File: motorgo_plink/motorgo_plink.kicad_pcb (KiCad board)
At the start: 4 copper layers, 65.2 x 56 mm, 0 parts

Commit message: WIP update. Layout begin
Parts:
- added C1: DNP, Capacitor_SMD:C_0402_1005Metric, F.Cu at (16.8, 80.9)
- added C10: 100uF, Capacitor_SMD:C_1210_3225Metric, F.Cu at (125.4, 105.6)
- added C11: 0.1uF, Capacitor_SMD:C_0402_1005Metric, B.Cu at (153.5, 107.1)
- added C12: 0.1uF, Capacitor_SMD:C_0402_1005Metric, B.Cu at (153.4, 108.1)
- added C13: .022uF, Capacitor_SMD:C_0402_1005Metric, B.Cu at (153.0, 105.6)
- added C14: 100uF, Capacitor_SMD:C_1210_3225Metric, F.Cu at (154.6, 105.6)
- added C15: 10uF 4mOhm, Capacitor_SMD:C_0805_2012Metric, F.Cu at (157.9, 85.0)
- added C16: 220uF 50v, Capacitor_SMD:CP_Elec_10x10, F.Cu at (52.7, 67.8)
- added C17: 4.7uF 1mOhm, Capacitor_SMD:C_0603_1608Metric, F.Cu at (152.4, 86.4)
- added C18: 2.2nF 0Ohm, Capacitor_SMD:C_0201_0603Metric, F.Cu at (161.3, 84.4)
- added C2: DNP, Capacitor_SMD:C_0402_1005Metric, F.Cu at (16.8, 82.9)
- added C20: 43pF 0Ohm, Capacitor_SMD:C_0201_0603Metric, F.Cu at (161.3, 86.2)
- added C21: 1uF, Capacitor_SMD:C_0603_1608Metric, F.Cu at (165.0, 98.3)
- added C22: 100nf 280mOhm, Capacitor_SMD:C_0402_1005Metric, F.Cu at (148.9, 84.3)
- added C23: 47uF 1mOhm, Capacitor_SMD:C_1210_3225Metric, F.Cu at (158.5, 81.4)
- added C24: 22uF 16v, Capacitor_SMD:C_0603_1608Metric, F.Cu at (135.8, 91.7)
- added C25: 22uF 16v, Capacitor_SMD:C_0603_1608Metric, F.Cu at (135.7, 94.7)
- added C26: 0.1uF, Capacitor_SMD:C_0402_1005Metric, B.Cu at (168.1, 107.1)
- added C27: 0.1uF, Capacitor_SMD:C_0402_1005Metric, B.Cu at (168.1, 108.1)
- added C28: .022uF, Capacitor_SMD:C_0402_1005Metric, B.Cu at (167.6, 105.6)
- added C29: 100uF, Capacitor_SMD:C_1210_3225Metric, F.Cu at (169.2, 105.6)
- added C3: 0.1uF, Capacitor_SMD:C_0402_1005Metric, B.Cu at (139.0, 107.1)
- added C30: 100nF, Capacitor_SMD:C_01005_0402Metric, F.Cu at (81.7, 38.1)
- added C31: 100nF, Capacitor_SMD:C_01005_0402Metric, F.Cu at (81.7, 39.7)
- added C32: 1uF, Capacitor_SMD:C_0603_1608Metric, F.Cu at (70.5, 48.4)
- added C4: 0.1uF, Capacitor_SMD:C_0402_1005Metric, B.Cu at (139.0, 108.1)
- added C5: .022uF, Capacitor_SMD:C_0402_1005Metric, B.Cu at (138.6, 105.6)
- added C6: 100uF, Capacitor_SMD:C_1210_3225Metric, F.Cu at (140.2, 105.6)
- added C7: 0.1uF, Capacitor_SMD:C_0402_1005Metric, B.Cu at (124.3, 107.1)
- added C8: 0.1uF, Capacitor_SMD:C_0402_1005Metric, B.Cu at (124.3, 108.1)
- added C9: .022uF, Capacitor_SMD:C_0402_1005Metric, B.Cu at (123.8, 105.6)
- added D1: LED, LED_SMD:LED_0805_2012Metric, F.Cu at (38.3, 77.7)
- added D2: LED, LED_SMD:LED_0805_2012Metric, F.Cu at (38.3, 80.8)
- added D3: LED, LED_SMD:LED_0805_2012Metric, F.Cu at (38.3, 83.8)
- added J1: USB4520-03-0-A_REVA, mg_mini_v1r3:GCT_USB4520-03-0-A_REVA, F.Cu at (172.5, 77.8)
- added J10: Conn_01x02_Pin, Connector_PinHeader_2.54mm:PinHeader_1x02_P2.54mm_Vertical, F.Cu at (143.8, 114.1)
- added J11: ~, LCSC_parts:CONN-TH_DC-005-2.5A-2.0, F.Cu at (120.7, 97.8)
- added J12: USB4520-03-0-A_REVA, mg_mini_v1r3:GCT_USB4520-03-0-A_REVA, F.Cu at (172.4, 94.5)
- added J13: I2C_STANDARDQWIIC, Connector_JST:JST_SH_BM04B-SRSS-TB_1x04-1MP_P1.00mm_Vertical, F.Cu at (29.1, 90.5)
- added J14: BM05B-SRSS-TB_LF__SN_, SnapEDA Library:JST_BM05B-SRSS-TB_LF__SN_, F.Cu at (119.4, 114.7)
- added J15: I2C_STANDARDQWIIC, Connector_JST:JST_SH_BM04B-SRSS-TB_1x04-1MP_P1.00mm_Vertical, F.Cu at (29.1, 96.7)
- added J16: BM05B-SRSS-TB_LF__SN_, SnapEDA Library:JST_BM05B-SRSS-TB_LF__SN_, F.Cu at (133.9, 114.7)
- added J17: I2C_STANDARDQWIIC, Connector_JST:JST_SH_BM04B-SRSS-TB_1x04-1MP_P1.00mm_Vertical, F.Cu at (29.1, 103.0)
- added J18: BM05B-SRSS-TB_LF__SN_, SnapEDA Library:JST_BM05B-SRSS-TB_LF__SN_, F.Cu at (149.8, 114.7)
- added J19: I2C_STANDARDQWIIC, Connector_JST:JST_SH_BM04B-SRSS-TB_1x04-1MP_P1.00mm_Vertical, F.Cu at (29.1, 109.2)
- added J2: ~, Button_Switch_SMD:SW_SPST_TL3342, F.Cu at (40.9, 55.7)
- added J20: BM05B-SRSS-TB_LF__SN_, SnapEDA Library:JST_BM05B-SRSS-TB_LF__SN_, F.Cu at (164.5, 114.7)
- added J22: Conn_01x02_Pin, Connector_PinHeader_2.54mm:PinHeader_1x02_P2.54mm_Vertical, F.Cu at (158.4, 114.1)
- added J23: Conn_01x06_Pin, Connector_PinHeader_1.00mm:PinHeader_1x06_P1.00mm_Vertical, F.Cu at (78.9, 38.8)
- added J3: ~, Button_Switch_SMD:SW_SPST_TL3342, F.Cu at (40.9, 62.8)
- added J4: Conn_02x20_Odd_Even, Connector_PinHeader_2.54mm:PinHeader_2x20_P2.54mm_Vertical_SMD, F.Cu at (142.2, 64.0)
- added J4: Conn_02x20_Odd_Even, Connector_PinHeader_2.54mm:PinHeader_2x20_P2.54mm_Vertical_SMD, B.Cu at (142.2, 64.0)
- added J6: Conn_01x02_Pin, Connector_PinHeader_2.54mm:PinHeader_1x02_P2.54mm_Vertical, F.Cu at (139.9, 114.1)
- added J8: Conn_01x02_Pin, Connector_PinHeader_2.54mm:PinHeader_1x02_P2.54mm_Vertical, F.Cu at (125.4, 114.1)
- added JP1: DNP, Jumper:SolderJumper-2_P1.3mm_Open_RoundedPad1.0x1.5mm, F.Cu at (47.8, 54.0)
- added JP2: DNP, Jumper:SolderJumper-2_P1.3mm_Open_RoundedPad1.0x1.5mm, F.Cu at (47.8, 57.5)
- added JP3: DNP, Jumper:SolderJumper-2_P1.3mm_Open_RoundedPad1.0x1.5mm, F.Cu at (47.8, 61.1)
- added JP4: SolderJumper_2_Bridged, Jumper:SolderJumper-2_P1.3mm_Bridged2Bar_RoundedPad1.0x1.5mm, F.Cu at (164.7, 90.3)
- added JP5: SolderJumper_2_Open, Jumper:SolderJumper-2_P1.3mm_Open_RoundedPad1.0x1.5mm, F.Cu at (162.1, 90.3)
- added JP6: SolderJumper_2_Open, Jumper:SolderJumper-2_P1.3mm_Open_RoundedPad1.0x1.5mm, F.Cu at (159.4, 90.3)
- added L1: 3.3uH 14mOhm, LCSC_parts:IND-SMD_L7.3-W6.6, F.Cu at (155.4, 75.3)
- added Q1: SI2323, LCSC_parts:SI2323_SOT-23-3_L2.9-W1.3-P0.95-LS2.4-BR, F.Cu at (162.4, 98.1)
- added R1: 1k, Resistor_SMD:R_0402_1005Metric, F.Cu at (42.0, 77.2)
- added R10: 10k, Resistor_SMD:R_0402_1005Metric, B.Cu at (128.8, 107.3)
- added R11: 10k, Resistor_SMD:R_0402_1005Metric, B.Cu at (128.9, 106.3)
- added R12: 10k, Resistor_SMD:R_0402_1005Metric, B.Cu at (114.1, 107.3)
- added R13: 10k, Resistor_SMD:R_0402_1005Metric, B.Cu at (114.1, 106.3)
- added R14: 10k, Resistor_SMD:R_0402_1005Metric, B.Cu at (143.3, 107.3)
- added R15: 10k, Resistor_SMD:R_0402_1005Metric, B.Cu at (143.3, 106.3)
- added R16: 102k, Resistor_SMD:R_0402_1005Metric, F.Cu at (148.9, 72.4)
- added R17: 36.5k, Resistor_SMD:R_0402_1005Metric, F.Cu at (148.9, 74.4)
- added R18: 53.6k, Resistor_SMD:R_0402_1005Metric, F.Cu at (148.9, 76.4)
- added R19: 3.4k, Resistor_SMD:R_0402_1005Metric, F.Cu at (148.9, 78.3)
- added R2: 1k, Resistor_SMD:R_0402_1005Metric, F.Cu at (42.0, 79.2)
- added R20: 10R 1%, Resistor_SMD:R_0402_1005Metric, F.Cu at (164.1, 96.1)
- added R21: DNP, Resistor_SMD:R_0402_1005Metric, F.Cu at (150.3, 97.7)
- added R22: DNP, Resistor_SMD:R_0402_1005Metric, F.Cu at (152.3, 97.7)
- added R23: 5.1K, Resistor_SMD:R_0402_1005Metric, F.Cu at (160.5, 99.2)
- added R24: 52.3k, Resistor_SMD:R_0402_1005Metric, F.Cu at (148.9, 80.3)
- added R25: 10k, Resistor_SMD:R_0402_1005Metric, F.Cu at (148.9, 82.3)
- added R26: 49.9K, Resistor_SMD:R_0402_1005Metric, F.Cu at (160.0, 97.7)
- added R27: 10K, Resistor_SMD:R_0402_1005Metric, F.Cu at (164.8, 87.8)
- added R28: 14K, Resistor_SMD:R_0402_1005Metric, F.Cu at (162.1, 87.8)
- added R29: 10.5K, Resistor_SMD:R_0402_1005Metric, F.Cu at (159.3, 87.8)
- added R3: 1k, Resistor_SMD:R_0402_1005Metric, F.Cu at (42.0, 81.2)
- added R30: 5k1, Resistor_SMD:R_0402_1005Metric, F.Cu at (35.0, 88.3)
- added R31: 5k1, Resistor_SMD:R_0402_1005Metric, F.Cu at (35.0, 90.3)
- added R32: 5k1, Resistor_SMD:R_0402_1005Metric, F.Cu at (35.0, 92.3)
- added R33: 5k1, Resistor_SMD:R_0402_1005Metric, F.Cu at (35.0, 94.3)
- added R34: 5k1, Resistor_SMD:R_0402_1005Metric, F.Cu at (35.0, 96.3)
- added R35: 5k1, Resistor_SMD:R_0402_1005Metric, F.Cu at (35.0, 98.3)
- added R36: 10k, Resistor_SMD:R_0402_1005Metric, B.Cu at (157.9, 107.3)
- added R37: 10k, Resistor_SMD:R_0402_1005Metric, B.Cu at (157.9, 106.3)
- added R38: 2k, Resistor_SMD:R_0402_1005Metric, F.Cu at (69.9, 38.2)
- added R39: 2k, Resistor_SMD:R_0402_1005Metric, F.Cu at (69.9, 40.2)
- added R4: 5k1, Resistor_SMD:R_0402_1005Metric, F.Cu at (44.9, 77.2)
- added R40: DNP, Resistor_SMD:R_0402_1005Metric, F.Cu at (69.9, 42.2)
- added R41: DNP, Resistor_SMD:R_0402_1005Metric, F.Cu at (69.9, 44.2)
- added R42: DNP, Resistor_SMD:R_0402_1005Metric, F.Cu at (69.9, 46.2)
- added R43: DNP, Resistor_SMD:R_0402_1005Metric, F.Cu at (72.8, 38.2)
- added R44: DNP, Resistor_SMD:R_0402_1005Metric, F.Cu at (72.8, 40.2)
- added R45: DNP, Resistor_SMD:R_0402_1005Metric, F.Cu at (72.8, 42.2)
- added R46: 1k, Resistor_SMD:R_0402_1005Metric, F.Cu at (72.8, 44.2)
- added R47: DNP, Resistor_SMD:R_0402_1005Metric, F.Cu at (72.8, 46.2)
- added R48: DNP, Resistor_SMD:R_0402_1005Metric, F.Cu at (75.7, 38.2)
- added R49: 1k, Resistor_SMD:R_0402_1005Metric, F.Cu at (75.7, 40.2)
- added R5: 5k1, Resistor_SMD:R_0402_1005Metric, F.Cu at (44.9, 79.2)
- added R50: 1k, Resistor_SMD:R_0402_1005Metric, F.Cu at (75.7, 42.2)
- added R6: 0, Resistor_SMD:R_0402_1005Metric, F.Cu at (44.9, 81.2)
- added R7: 0, Resistor_SMD:R_0402_1005Metric, F.Cu at (47.8, 77.2)
- added R8: 5k1, Resistor_SMD:R_0402_1005Metric, F.Cu at (47.8, 79.2)
- added R9: 5k1, Resistor_SMD:R_0402_1005Metric, F.Cu at (47.8, 81.2)
- added Rmode1: 20k, Resistor_SMD:R_0402_1005Metric, B.Cu at (128.8, 109.3)
- added Rmode2: 20k, Resistor_SMD:R_0402_1005Metric, B.Cu at (114.1, 109.3)
- added Rmode3: 20k, Resistor_SMD:R_0402_1005Metric, B.Cu at (143.3, 109.3)
- added Rmode4: 20k, Resistor_SMD:R_0402_1005Metric, B.Cu at (157.9, 109.3)
- added Rp1: 4.83k, Resistor_SMD:R_0402_1005Metric, B.Cu at (128.8, 108.3)
- added Rp2: 4.83k, Resistor_SMD:R_0402_1005Metric, B.Cu at (114.1, 108.3)
- added Rp3: 4.83k, Resistor_SMD:R_0402_1005Metric, B.Cu at (143.3, 108.3)
- added Rp4: 4.83k, Resistor_SMD:R_0402_1005Metric, B.Cu at (157.9, 108.3)
- added TP1: TestPoint, TestPoint:TestPoint_Pad_1.0x1.0mm, F.Cu at (133.2, 102.1)
- added TP10: TestPoint, TestPoint:TestPoint_Pad_1.0x1.0mm, F.Cu at (122.6, 102.1)
- added TP11: TestPoint, TestPoint:TestPoint_Pad_1.0x1.0mm, F.Cu at (151.8, 102.1)
- added TP12: TestPoint, TestPoint:TestPoint_Pad_1.0x1.0mm, F.Cu at (166.4, 102.1)
- added TP2: TestPoint, TestPoint:TestPoint_Pad_1.0x1.0mm, F.Cu at (118.5, 102.1)
- added TP3: TestPoint, TestPoint:TestPoint_Pad_1.0x1.0mm, F.Cu at (147.6, 102.1)
- added TP4: TestPoint, TestPoint:TestPoint_Pad_1.0x1.0mm, F.Cu at (162.3, 102.1)
- added TP5: TestPoint, TestPoint:TestPoint_Pad_1.0x1.0mm, F.Cu at (135.3, 102.1)
- added TP6: TestPoint, TestPoint:TestPoint_Pad_1.0x1.0mm, F.Cu at (120.5, 102.1)
- added TP7: TestPoint, TestPoint:TestPoint_Pad_1.0x1.0mm, F.Cu at (149.7, 102.1)
- added TP8: TestPoint, TestPoint:TestPoint_Pad_1.0x1.0mm, F.Cu at (164.3, 102.1)
- added TP9: TestPoint, TestPoint:TestPoint_Pad_1.0x1.0mm, F.Cu at (137.4, 102.1)
- added U1: ESP32-S3-WROOM-1, mg_mini_v1r3:ESP32-S3-WROOM-1, F.Cu at (122.8, 80.3)
- added U10: LIS3MDLTR, LCSC_parts:LIS3MDLTR_LGA-12, F.Cu at (74.3, 48.9)
- added U11: LSM6DS3TR, LCSC_parts:LSM6DSOTR_LGA-14, F.Cu at (79.2, 47.6)
- added U2: USBLC6-2P6, Package_TO_SOT_SMD:SOT-666, F.Cu at (163.7, 73.1)
- added U3: DRV8874PWPR, LCSC_parts:HTSSOP-16_L5.0-W4.4-P0.65-LS6.4-BL-EP, F.Cu at (134.3, 106.3)
- added U4: DRV8874PWPR, LCSC_parts:HTSSOP-16_L5.0-W4.4-P0.65-LS6.4-BL-EP, F.Cu at (119.6, 106.3)
- added U5: DRV8874PWPR, LCSC_parts:HTSSOP-16_L5.0-W4.4-P0.65-LS6.4-BL-EP, F.Cu at (148.7, 106.3)
- added U6: TPS54620RHLR, LCSC_parts:VQFN-14_L3.5-W3.5-P0.50-TL-EP_TPS54622RHLT, F.Cu at (153.0, 82.4)
- added U7: HUSB238_002DD, LCSC_parts:DFN-10_L3.0-W3.0-P0.50-BL-EP2.5, F.Cu at (163.5, 94.0)
- added U8: AMS1117-3.3, Package_TO_SOT_SMD:SOT-223-3_TabPin2, F.Cu at (130.5, 94.1)
- added U9: DRV8874PWPR, LCSC_parts:HTSSOP-16_L5.0-W4.4-P0.65-LS6.4-BL-EP, F.Cu at (163.4, 106.3)
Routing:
- net +3.3V: track 0.00 -> 62.9 mm, vias 0 -> 3
- net GND: track 0.00 -> 19.6 mm, vias 0 -> 8
- net /motor_controls4/motor_out1: track 0.00 -> 13.7 mm
- net +BATT: track 0.00 -> 12.4 mm, vias 0 -> 6
- net Net-(U9-PMODE): track 0.00 -> 10.0 mm, vias 0 -> 1
- net Net-(U9-nFAULT): track 0.00 -> 8.92 mm, vias 0 -> 3
- net +3V3: track 0.00 -> 8.57 mm, vias 0 -> 2
- net +VDC: track 0.00 -> 6.76 mm, vias 0 -> 3
- net Net-(U9-nSLEEP): track 0.00 -> 6.26 mm, vias 0 -> 2
- net Net-(U7-GATE): track 0.00 -> 6.18 mm
- net Net-(U9-IPROPI): track 0.00 -> 4.62 mm, vias 0 -> 1
- net Net-(U9-VCP): track 0.00 -> 3.95 mm, vias 0 -> 1
- net Net-(Q1-G): track 0.00 -> 3.87 mm
- net /motor_controls4/motor_out2: track 0.00 -> 3.79 mm
- net /Power Reg and Dist/CC1: track 0.00 -> 3.50 mm
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- added copper zone on In2.Cu, net +BATT
- added copper zone on In2.Cu, net +VDC
- added copper zone on In1.Cu, net GND
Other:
- board size 65.2 x 56 mm -> 80.2 x 56 mm

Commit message: WIP update. Ready for BOM editing
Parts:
- removed the J4 at (142.2, 64.0)
- removed R35: 5k1, Resistor_SMD:R_0402_1005Metric
- added J5: Conn_02x20_Odd_Even, Connector_PinSocket_2.54mm:PinSocket_2x20_P2.54mm_Vertical_SMD, B.Cu at (142.2, 64.0)
- J4: footprint Connector_PinHeader_2.54mm:PinHeader_2x20_P2.54mm_Vertical_SMD -> Connector_PinSocket_2.54mm:PinSocket_2x20_P2.54mm_Vertical_SMD
- R10, R11, R12, R13, R14, R15, R36, R37, Rmode1, Rmode2, Rmode3, Rmode4, Rp1, Rp2, Rp3, Rp4: moved to F.Cu
- R34: value 5k1 -> 0R0; footprint Resistor_SMD:R_0402_1005Metric -> Resistor_SMD:R_0603_1608Metric
- moved C2 142.9 mm to (159.6, 76.8)
- moved C1 142.8 mm to (159.6, 78.4)
- moved J3 122.5 mm to (161.6, 83.2)
- moved J2 121.9 mm to (161.6, 72.5)
- moved R4 119.1 mm to (164.0, 79.3)
- moved R5 119.0 mm to (163.9, 76.0)
- moved R6 117.0 mm to (161.9, 78.3)
- moved R34 114.9 mm to (148.2, 76.2)
- moved R7 114.0 mm to (161.9, 77.1)
- moved R8 109.0 mm to (156.7, 74.7), turned to 90 degrees
- moved R9 109.0 mm to (156.8, 81.1), turned to 90 degrees
- moved R32 101.1 mm to (134.5, 110.4)
- moved R33 98.7 mm to (132.4, 110.3), turned to 180 degrees
- moved D1 95.5 mm to (133.6, 84.0), turned to 180 degrees
- moved D3 95.3 mm to (133.6, 86.6), turned to 180 degrees
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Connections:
- C30 pad 1: GND -> GNDD
- C31 pad 1: +3V3 -> +3.3V
- C31 pad 2: GND -> GNDD
- C32 pad 1: +3V3 -> +3.3V
- C32 pad 2: GND -> GNDD
- R21 pad 1: +3V3 -> +3.3V
- R22 pad 1: +3V3 -> +3.3V
- R34 pad 1: +3.3V -> GNDD
- R34 pad 2: sda -> GND
- R38 pad 1: +3V3 -> +3.3V
- R39 pad 1: +3V3 -> +3.3V
- R40 pad 2: GND -> GNDD
- R41 pad 2: GND -> GNDD
- R42 pad 2: GND -> GNDD
- R43 pad 2: GND -> GNDD
- R44 pad 2: GND -> GNDD
- R45 pad 2: GND -> GNDD
- R46 pad 2: GND -> GNDD
- R47 pad 2: +3V3 -> +3.3V
- R48 pad 2: +3V3 -> +3.3V
- R49 pad 2: GND -> GNDD
- R50 pad 2: +3V3 -> +3.3V
- TP10 pad 1: +3V3 -> +3.3V
- TP11 pad 1: +3V3 -> +3.3V
- TP12 pad 1: +3V3 -> +3.3V
- TP9 pad 1: +3V3 -> +3.3V
- U10 pad 10: +3V3 -> +3.3V
- U10 pad 12: GND -> GNDD
- U10 pad 2: GND -> GNDD
- U10 pad 3: GND -> GNDD
- U10 pad 5: +3V3 -> +3.3V
- U10 pad 6: +3V3 -> +3.3V
- U11 pad 5: +3V3 -> +3.3V
- U11 pad 6: GND -> GNDD
- U11 pad 7: GND -> GNDD
- U11 pad 8: +3V3 -> +3.3V
- U3 pad 5: +3V3 -> +3.3V
- U4 pad 5: +3V3 -> +3.3V
- U5 pad 5: +3V3 -> +3.3V
- U6 pad 15: unconnected-(U6-EP-Pad15) -> GND
- U9 pad 5: +3V3 -> +3.3V
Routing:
- net +5V: track 3.47 -> 92.5 mm, vias 0 -> 16
- net enc_sda: track 0.00 -> 73.6 mm, vias 0 -> 5
- net GND: track 19.6 -> 93.0 mm, vias 8 -> 52
- net enc_scl: track 0.00 -> 70.4 mm, vias 0 -> 5
- net usb_d-: track 0.00 -> 55.5 mm, vias 0 -> 2
- net +BATT: track 12.4 -> 67.4 mm, vias 6 -> 21
- net +3.3V: track 62.9 -> 117.9 mm, vias 3 -> 18
- net usb_d+: track 0.00 -> 54.8 mm, vias 0 -> 2
- net m4_enc_cs: track 0.00 -> 52.1 mm, vias 0 -> 2
- net m4_PH: track 0.00 -> 41.5 mm, vias 0 -> 1
- net hidden_sda: track 0.00 -> 40.4 mm, vias 0 -> 7
- net m4_EN: track 0.00 -> 40.0 mm, vias 0 -> 1
- net hidden_scl: track 0.00 -> 38.9 mm, vias 0 -> 4
- net m3_enc_cs: track 0.00 -> 36.0 mm, vias 0 -> 1
- net m2_enc_cs: track 0.00 -> 29.8 mm, vias 0 -> 2
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- added copper zone on In2.Cu, net +3.3V
- added copper zone on In2.Cu, net +5V
- added copper zone on In1.Cu, net GNDD

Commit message: WIP update. change USBC port
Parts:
- removed J12: USB4520-03-0-A_REVA, mg_mini_v1r3:GCT_USB4520-03-0-A_REVA
- added D4: 20V 5A, LCSC_parts:D_SMB_LCSC_C5366311, B.Cu at (162.9, 96.3)
- added J7: USB4520-03-0-A_REVA, mg_mini_v1r3:USB-C-SMD_TYPEC-303-ACP16, F.Cu at (170.5, 94.2)
- J1: footprint mg_mini_v1r3:GCT_USB4520-03-0-A_REVA -> mg_mini_v1r3:USB-C-SMD_TYPEC-303-ACP16
- Rp1, Rp2, Rp3, Rp4: value 4.83k -> 4.87k
- moved R32 7.29 mm to (128.1, 113.9), turned to 90 degrees
- moved R33 4.86 mm to (129.1, 113.9), turned to 90 degrees
- moved R31 4.16 mm to (102.1, 108.0), turned to 180 degrees
- moved R30 2.40 mm to (102.1, 106.7), turned to 180 degrees
- moved J1 1.98 mm to (170.6, 77.5)
- moved R20 1.02 mm to (165.2, 96.1)
- moved R26 0.64 mm to (160.6, 97.7)
- moved Q1 0.45 mm to (162.7, 97.9), turned to 90 degrees
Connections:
- J4 pad 10: gpio43 -> gpio44
- J4 pad 8: gpio44 -> gpio43
- J5 pad 7: gpio44 -> gpio43
- J5 pad 9: gpio43 -> gpio44
- Q1 pad 2: +VDC -> Net-(D4-K)
- R26 pad 1: +VDC -> Net-(D4-K)
- U1 pad 10: m3_PH -> m2_PH
- U1 pad 11: m4_EN -> m2_EN
- U1 pad 12: gpio8 -> m3_PH
- U1 pad 15: gpio3 -> m3_EN
- U1 pad 17: gpio9 -> m3_enc_cs
- U1 pad 18: m1_EN -> m4_PH
- U1 pad 19: m1_PH -> m4_EN
- U1 pad 20: m2_EN -> m4_enc_cs
- U1 pad 21: m2_PH -> hidden_sda
- U1 pad 22: m3_EN -> hidden_scl
- U1 pad 23: m4_PH -> gpio38
- U1 pad 24: gpio47 -> gpio41
- U1 pad 25: m2_enc_cs -> gpio42
- U1 pad 28: enc_sda -> gpio4
- U1 pad 29: enc_scl -> gpio7
- U1 pad 30: m1_enc_cs -> gpio3
- U1 pad 31: gpio38 -> gpio8
- U1 pad 34: gpio41 -> gpio44
- U1 pad 35: gpio42 -> gpio47
- U1 pad 36: gpio44 -> gpio43
- U1 pad 37: gpio43 -> gpio9
- U1 pad 4: gpio4 -> m2_enc_cs
- U1 pad 5: hidden_scl -> m1_enc_cs
- U1 pad 6: hidden_sda -> enc_sda
- U1 pad 7: gpio7 -> enc_scl
- U1 pad 8: m3_enc_cs -> m1_PH
- U1 pad 9: m4_enc_cs -> m1_EN
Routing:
- net +3.3V: track 117.9 -> 211.8 mm, vias 18 -> 24
- net sda: track 0.00 -> 88.5 mm, vias 0 -> 5
- net scl: track 0.00 -> 85.5 mm, vias 0 -> 7
- net GND: track 93.0 -> 165.8 mm, vias 52 -> 75
- net boot: track 8.13 -> 64.4 mm, vias 0 -> 2
- net reset: track 8.29 -> 64.3 mm, vias 0 -> 2
- net gpio47: track 1.74 -> 55.3 mm, vias 0 -> 4
- net gpio38: track 5.40 -> 53.1 mm, vias 1 -> 4
- net gpio40: track 0.00 -> 47.1 mm, vias 0 -> 4
- net gpio39: track 0.00 -> 43.3 mm, vias 0 -> 2
- net gpio8: track 0.00 -> 35.3 mm, vias 0 -> 2
- net gpio41: track 0.00 -> 33.9 mm, vias 0 -> 2
- net gpio3: track 0.00 -> 31.4 mm, vias 0 -> 3
- net gpio42: track 0.00 -> 31.2 mm, vias 0 -> 2
- net hidden_sda: track 40.4 -> 69.6 mm, vias 7 -> 8
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- added copper zone on B.Cu, net +3.3V
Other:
- board size 80.2 x 56 mm -> 80.5 x 64.5 mm

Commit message: ready for order
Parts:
- removed C1, C2: DNP, Capacitor_SMD:C_0402_1005Metric
- moved C22 0.67 mm to (150.2, 90.8), turned to -90 degrees
- moved R17 0.37 mm to (153.0, 90.1)
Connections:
- J1 pad A12: (no net) -> GND
- J1 pad B1: (no net) -> GND
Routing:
- net +5V: track 118.0 -> 172.0 mm, vias 22 -> 26
- net +3.3V: track 211.8 -> 253.2 mm, vias 24 -> 29
- net GND: track 165.8 -> 191.3 mm, vias 75 -> 84
- net +BATT: track 66.6 -> 80.2 mm
- net Net-(C22-Pad1): track 0.50 -> 7.18 mm
- net gpio47: track 55.3 -> 56.8 mm
- net gpio38: track 53.1 -> 54.3 mm
- net gpio41: track 33.9 -> 34.6 mm
- net usb_d-: track 55.5 -> 55.0 mm
- net usb_d+: track 54.8 -> 54.2 mm
- net gpio40: track 47.1 -> 47.6 mm, vias 4 -> 3
- net gpio4: track 18.0 -> 17.7 mm, vias 2 -> 1
- net m4_EN: track 56.4 -> 56.6 mm, vias 2 -> 3
- net gpio42: vias 2 -> 1
- net gpio39: track 43.3 -> 43.4 mm, vias 2 -> 4
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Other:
- board text added: "Acc"
- board text added: "M3"
- board text added: "Mag"
- board text added: "X+"
- board text added: "Y+"
- board text added: "int1_a SDO_a int_mag"
- board text added: "int2_a drdy_mag SD0_mag"

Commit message: fix DRC errors
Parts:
- moved Rmode3 3.39 mm to (146.6, 109.9), turned to -135 degrees
- moved Rmode4 2.51 mm to (155.5, 110.2)
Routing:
- net +5V: track 172.0 -> 174.6 mm, vias 26 -> 23
- net Net-(U9-IMODE): track 2.86 -> 5.45 mm
- net GND: track 191.3 -> 190.5 mm, vias 84 -> 83
- net +3.3V: track 253.2 -> 252.7 mm
- net Net-(U5-IMODE): track 2.86 -> 2.35 mm
- net m4_EN: vias 3 -> 2

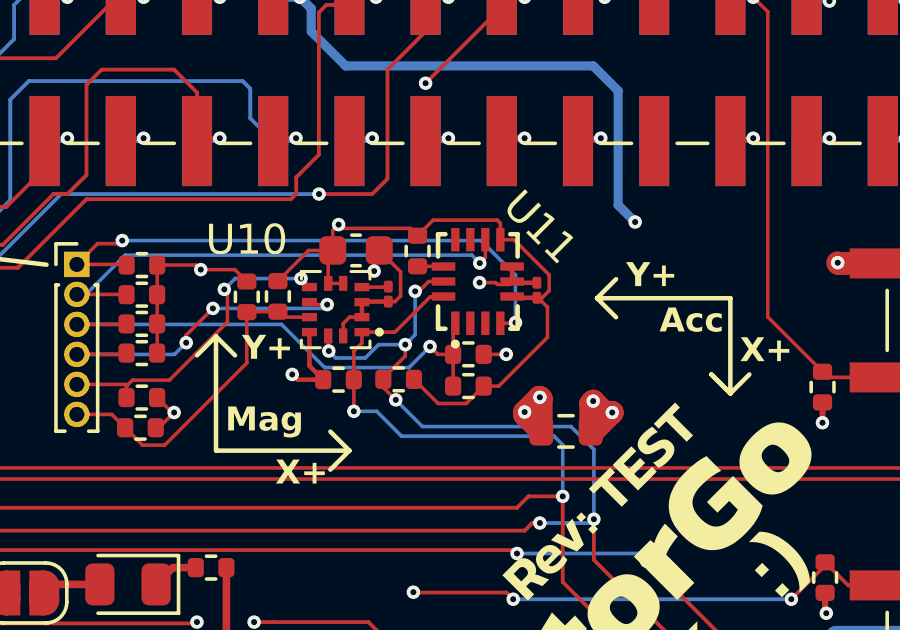
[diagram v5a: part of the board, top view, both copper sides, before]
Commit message: fix C31 and C30
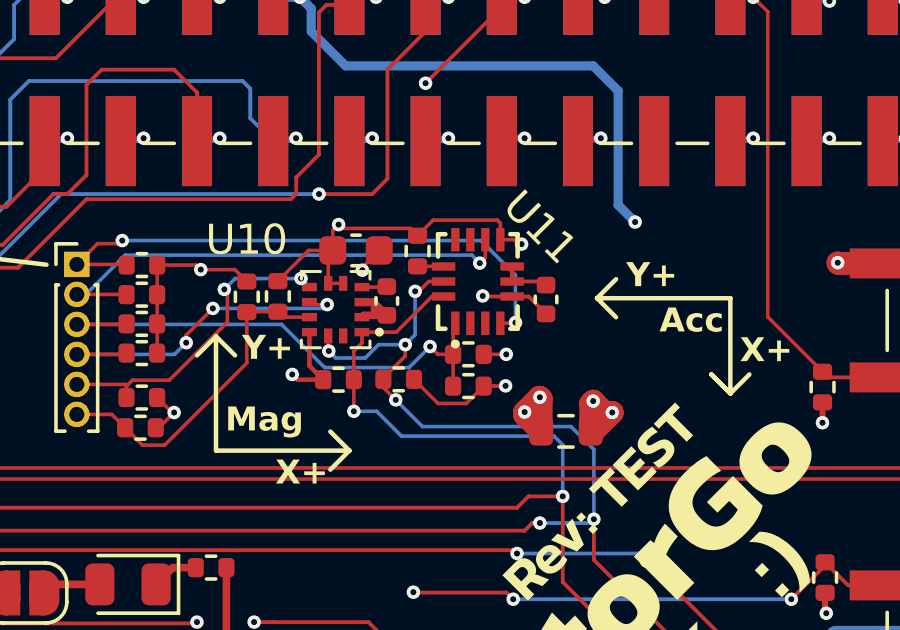
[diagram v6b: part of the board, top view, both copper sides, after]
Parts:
- C30, C31: footprint Capacitor_SMD:C_01005_0402Metric -> Capacitor_SMD:C_0402_1005Metric
- moved C31 0.43 mm to (147.5, 71.8)
- moved C30 0.23 mm to (142.2, 71.8)
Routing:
- net +3.3V: track 252.7 -> 248.3 mm, vias 29 -> 32
- net GNDD: track 19.8 -> 16.7 mm, vias 7 -> 6

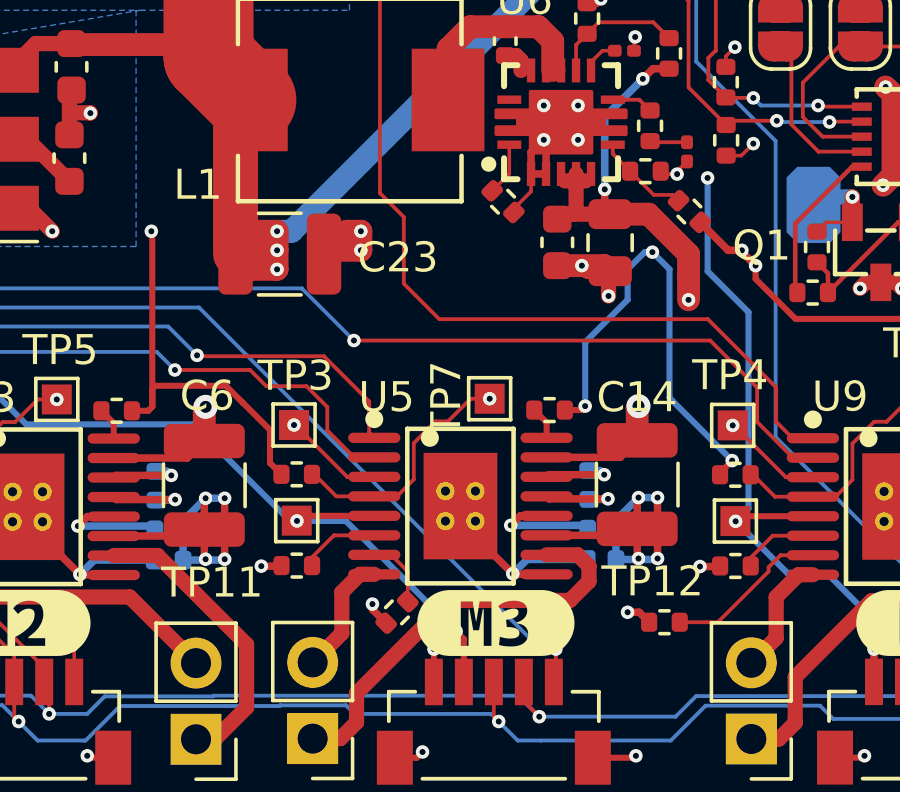
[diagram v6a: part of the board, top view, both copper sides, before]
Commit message: wip culling of non-vital schematic components
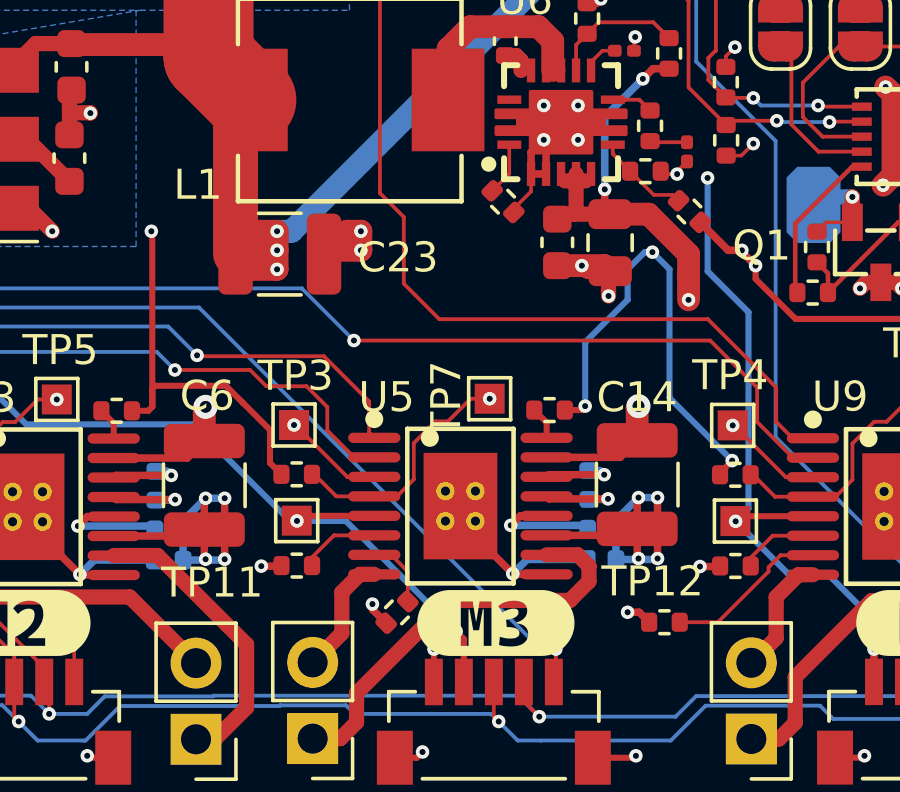
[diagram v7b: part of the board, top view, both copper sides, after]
